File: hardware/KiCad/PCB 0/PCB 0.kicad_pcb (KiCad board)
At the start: 2 copper layers, 59.6 x 59.6 mm, 0 parts

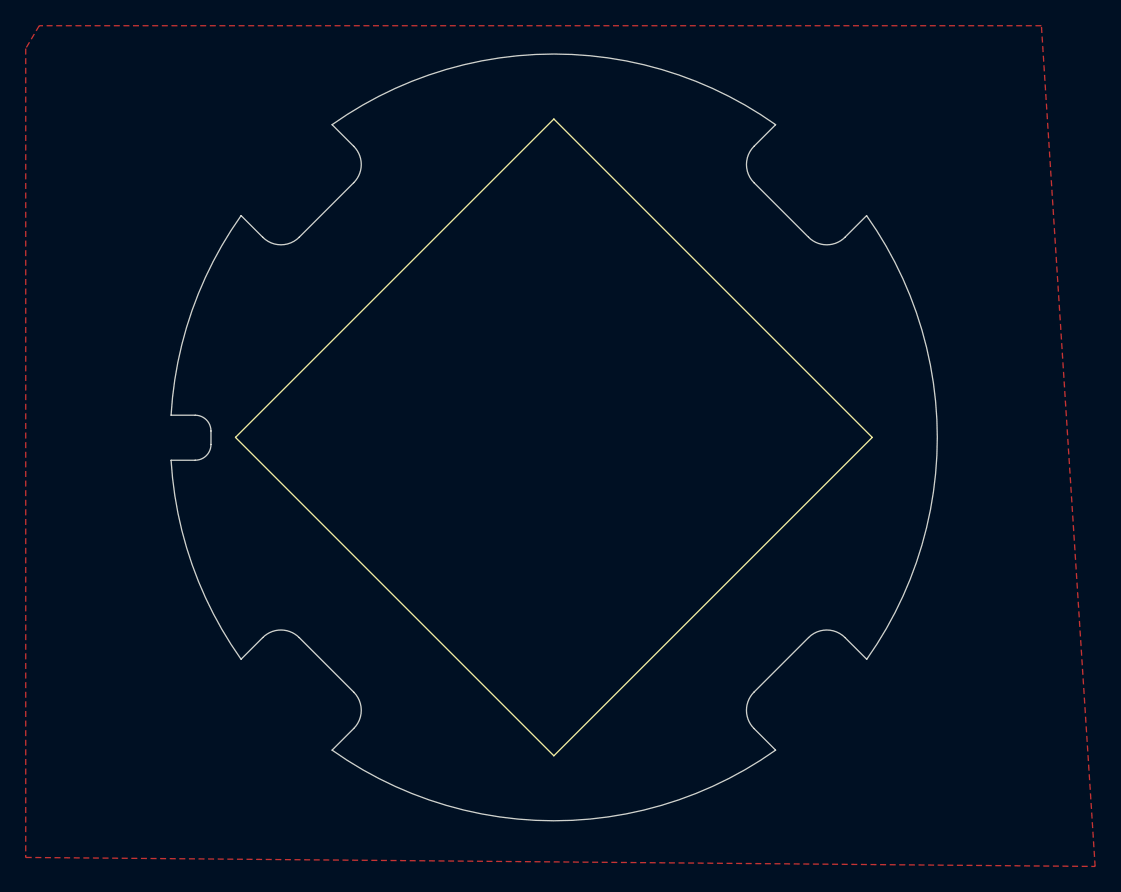
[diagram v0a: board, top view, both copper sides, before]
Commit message: Added 3D models for each PCB
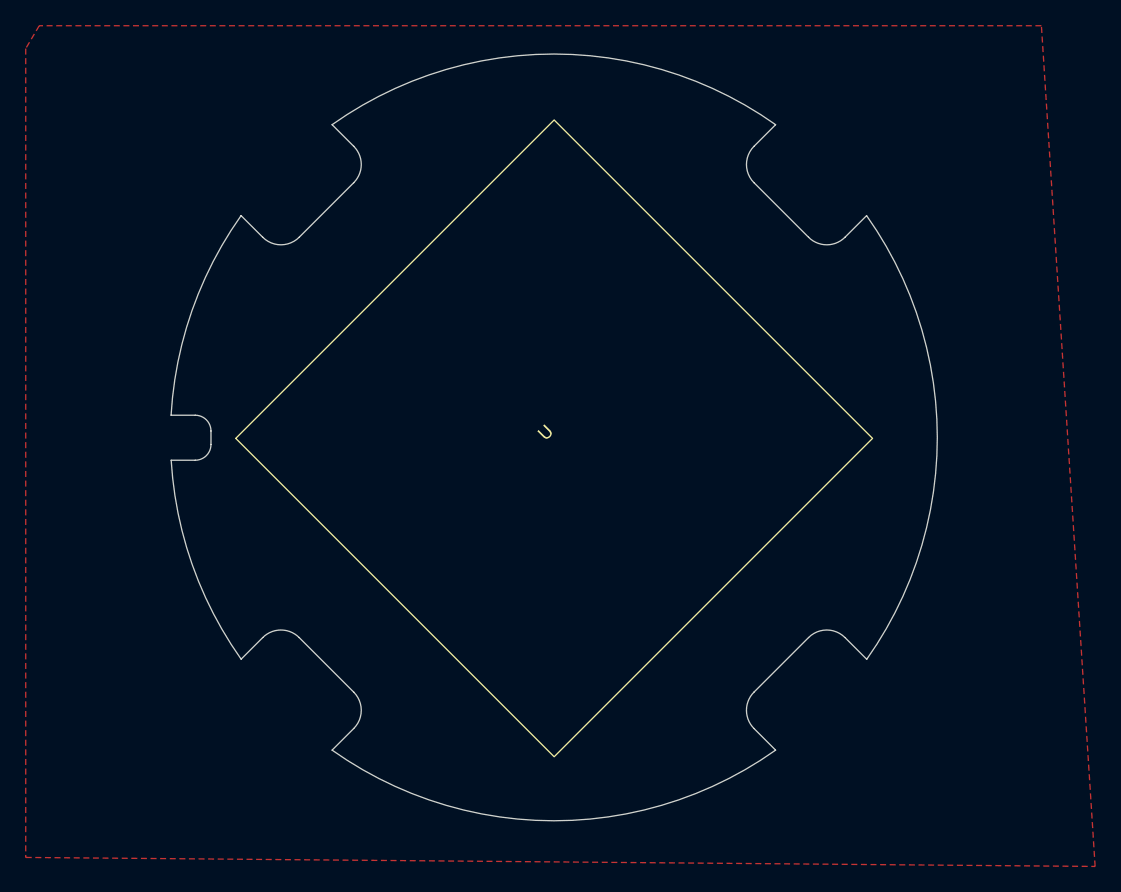
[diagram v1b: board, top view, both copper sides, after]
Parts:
- added U: AGVLB256.A.07.0100AO, AGVLB256.A.07.0100AO:AGVLB256.A.07.0100AO, F.Cu at (159.6, 91.2)
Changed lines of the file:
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@@
 	)
 	(net 0 "")
-	(gr_poly
-		(pts
-			(xy 135.103782 91.200026) (xy 159.852519 66.451289) (xy 184.601256 91.200026) (xy 159.852519 115.948763)
-		)
-		(stroke
-			(width 0.05)
-			(type solid)
-		)
-		(fill no)
-		(layer "F.SilkS")
+	(footprint "AGVLB256.A.07.0100AO:AGVLB256.A.07.0100AO"
+		(layer "F.Cu")
+		(at 159.57448 91.186612 45)
+		(property "Reference" "U"
+			(at 0 -0.499999 45)
+			(unlocked yes)
+			(layer "F.SilkS")
+			(effects
+				(font
+					(size 1 1)
+					(thickness 0.1)
+				)
+			)
+		)
+		(property "Value" "AGVLB256.A.07.0100AO"
+			(at 0 1 45)
+			(unlocked yes)
+			(layer "F.Fab")
+			(effects
+				(font
+					(size 1 1)
+					(thickness 0.15)
+				)
+			)
+		)
+		(property "Datasheet" ""
+			(at 0 0 45)
+			(unlocked yes)
+			(layer "F.Fab")
+			(hide yes)
+			(effects
+				(font
+					(size 1 1)
+					(thickness 0.15)
+				)
+			)
+		)
+		(property "Description" ""
+			(at 0 0 45)
+			(unlocked yes)
+			(layer "F.Fab")
+			(hide yes)
+			(effects
+				(font
+					(size 1 1)
+					(thickness 0.15)
+				)
+			)
+		)
+		(attr smd)
+		(fp_poly
+			(pts
+				(xy -17.35 -17.225) (xy 17.65 -17.225) (xy 17.65 17.775) (xy -17.35 17.775)
+			)
+			(stroke
+				(width 0.1)
+				(type default)
+			)
+			(fill no)
+			(layer "F.SilkS")
+		)
+		(fp_text user "${REFERENCE}"
+			(at 0 2.5 45)
+			(unlocked yes)
+			(layer "F.Fab")
+			(effects
+				(font
+					(size 1 1)
+					(thickness 0.15)
+				)
+			)
+		)
+		(embedded_fonts no)
+		(model "/Users/kuba/Documents/GitHub/AeroTrackNow/hardware/KiCad/Libaries/AGVLB256.A.07.0100AO.pretty/AGVLB256.A.07.0100AO_Web.STEP"
+			(offset
+				(xyz 357.5 -418 3.5)
+			)
+			(scale
+				(xyz 1 1 1)
+			)
+			(rotate
+				(xyz -0 -180 -0)
+			)
+		)
 	)
 	(gr_line
@@
 	)
 	(gr_arc
-		(start 135.53744 108.442137)
-		(mid 131.733076 101.089956)
-		(end 130.097459 92.975)
+		(start 135.543948 108.437524)
+		(mid 131.740598 101.087311)
+		(end 130.105417 92.974525)
 		(stroke
 			(width 0.05)
@@
 	)
 	(gr_line
-		(start 131.975 89.475)
+		(start 131.975 89.475703)
 		(end 130.097459 89.475)
 		(stroke
@@
 	)
 	(gr_line
-		(start 131.975 92.975)
-		(end 130.097459 92.975)
+		(start 131.975 92.974297)
+		(end 130.105417 92.974525)
 		(stroke
 			(width 0.05)
@@
 	(gr_line
 		(start 137.225124 75.643652)
-		(end 135.543948 73.962476)
+		(end 135.539826 73.959552)
 		(stroke
 			(width 0.05)
@@
 		)
 	)
-	(group ""
-		(members "08420494-acae-4cb6-b326-e4ec070ceaf3" "0874ac52-5748-4b44-a42b-39c7dd0e0d57"
-			"187c21d6-b81d-414a-9478-8a24abd201f2" "25520365-3cfc-4063-9ba6-c8a53d1a99ec"
-			"2c1db930-8e98-4a40-907d-efec6362c9b9" "2c858422-98ac-4b91-a749-b69f62f56b58"
-			"318abbf7-6ec9-4667-b46f-09b83ca430a0" "32ed5a8b-d3d5-4f88-a69a-5bfa9e14f704"
-			"3a6c4926-e2cc-405c-9a9d-de3e5c4a7e07" "451bfbaa-d56b-4422-830a-6ed66245e663"
-			"50ac55ce-af95-4228-92ae-1eef703e2e83" "54ac7e0c-4441-4b64-93c2-e85b231f5f50"
-			"5d94fd95-9c2e-4fd7-9aa7-9692d225dfb3" "6633e524-60eb-4d9c-949a-830a09ebdfe7"
-			"66ec3ab0-8199-4804-8dc8-77620aa3b0fb" "6f40bb01-fddc-4e29-99e8-5e5807d9427a"
-			"7293536b-0a75-4c20-b26b-3f0fc488779b" "8e0a516f-f613-40b9-9249-84a6b74ba839"
-			"92b5f240-f942-4c7f-b663-f64fbd003541" "a084cc9a-2d67-4f3d-8032-c9ba6d9a4095"
-			"a0a0bd65-b596-4a53-8b01-b0b236ea6360" "a87c5d81-3f74-4050-9fac-efd929fc7d35"
-			"abc2d670-1d08-49e9-b30b-091774b2664b" "abeb46d6-94b1-4bf1-9ad8-ccdb2ea2cbc0"
-			"b75e9c8c-f783-4949-86e9-5ca86a7d7ce0" "c01f7486-24aa-4c96-80d5-0f3f39423ac7"
-			"ccfeb74e-9815-4f51-b051-d2d05180265d" "d2d00f83-dec7-438c-a761-8b60de42d363"
-			"d5bca7a1-e69a-4310-8d2f-d1815de8b18c" "f802abe9-49d3-4fe6-a8fe-16165a57880c"
-		)
-	)
